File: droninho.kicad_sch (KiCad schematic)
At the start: 36 parts, among them J2 M2, J3 M1, J4 M3, J5 M4, J6 I2C, J7 TXD0/RXD0, J8 I2C, Q1 SI2300, Q2 SI2300, Q3 SI2300, Q4 SI2300, U1 AMS1117-3.3, U2 MPU9250/6500, U3 ESP32 Dev Kit

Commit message: update
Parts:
- removed H1, H2: MountingHole_Pad_Power, MountingHole:MountingHole_2.2mm_M2_Pad_TopBottom, symbol Mechanical:MountingHole_Pad_Power
- added H3, H4: MountingHole_Pad_Power, MountingHole:MountingHole_2.2mm_M2_Pad_TopBottom, symbol Library:MountingHole_Pad_Power
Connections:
- net BAT+: now also H3.1
- net GND: now also H4.1
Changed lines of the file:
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@@
-	)
-	(symbol
-		(lib_id "Mechanical:MountingHole_Pad_Power")
-		(at 34.29 91.44 90)
-		(unit 1)
-		(exclude_from_sim yes)
-		(in_bom no)
-		(on_board yes)
-		(dnp no)
-		(fields_autoplaced yes)
-		(property "Reference" "H1"
-			(at 33.02 85.09 90)
-			(effects
-				(font
-					(size 1.27 1.27)
-				)
-			)
-		)
-		(property "Value" "MountingHole_Pad_Power"
-			(at 33.02 87.63 90)
-			(effects
-				(font
-					(size 1.27 1.27)
-				)
-			)
-		)
-		(property "Footprint" "MountingHole:MountingHole_2.2mm_M2_Pad_TopBottom"
-			(at 34.29 91.44 0)
-			(effects
-				(font
-					(size 1.27 1.27)
-				)
-				(hide yes)
-			)
-		)
-		(property "Datasheet" "~"
-			(at 34.29 91.44 0)
-			(effects
-				(font
-					(size 1.27 1.27)
-				)
-				(hide yes)
-			)
-		)
-		(property "Description" "Mounting Hole with connection"
-			(at 34.29 91.44 0)
-			(effects
-				(font
-					(size 1.27 1.27)
-				)
-				(hide yes)
-			)
-		)
-		(pin "1"
-		)
-		(instances
-			(project ""
-				(path "/50215636-8ce2-4b01-ade7-3715bffabe9d"
-					(reference "H1")
-					(unit 1)
-				)
-			)
-		)
 	)
 	(symbol
@@
 	)
 	(symbol
+		(lib_id "Library:MountingHole_Pad_Power")
+		(at 34.29 104.14 90)
+		(unit 1)
+		(exclude_from_sim no)
+		(in_bom no)
+		(on_board yes)
+		(dnp no)
+		(fields_autoplaced yes)
+		(property "Reference" "H4"
+			(at 33.02 97.79 90)
+			(effects
+				(font
+					(size 1.27 1.27)
+				)
+			)
+		)
+		(property "Value" "MountingHole_Pad_Power"
+			(at 33.02 100.33 90)
+			(effects
+				(font
+					(size 1.27 1.27)
+				)
+			)
+		)
+		(property "Footprint" "MountingHole:MountingHole_2.2mm_M2_Pad_TopBottom"
+			(at 34.29 104.14 0)
+			(effects
+				(font
+					(size 1.27 1.27)
+				)
+				(hide yes)
+			)
+		)
+		(property "Datasheet" "~"
+			(at 34.29 104.14 0)
+			(effects
+				(font
+					(size 1.27 1.27)
+				)
+				(hide yes)
+			)
+		)
+		(property "Description" "Mounting Hole with connection"
+			(at 34.29 104.14 0)
+			(effects
+				(font
+					(size 1.27 1.27)
+				)
+				(hide yes)
+			)
+		)
+		(pin "1"
+		)
+		(instances
+			(project "droninho"
+				(path "/50215636-8ce2-4b01-ade7-3715bffabe9d"
+					(reference "H4")
+					(unit 1)
+				)
+			)
+		)
+	)
+	(symbol
 		(lib_id "power:GND")
 		(at 29.21 55.88 0)
@@
 	)
 	(symbol
-		(lib_id "Mechanical:MountingHole_Pad_Power")
-		(at 34.29 104.14 90)
-		(unit 1)
-		(exclude_from_sim yes)
-		(in_bom no)
-		(on_board yes)
-		(dnp no)
-		(fields_autoplaced yes)
-		(property "Reference" "H2"
-			(at 33.02 97.79 90)
-			(effects
-				(font
-					(size 1.27 1.27)
-				)
-			)
-		)
-		(property "Value" "MountingHole_Pad_Power"
-			(at 33.02 100.33 90)
-			(effects
-				(font
-					(size 1.27 1.27)
-				)
-			)
-		)
-		(property "Footprint" "MountingHole:MountingHole_2.2mm_M2_Pad_TopBottom"
-			(at 34.29 104.14 0)
-			(effects
-				(font
-					(size 1.27 1.27)
-				)
-				(hide yes)
-			)
-		)
-		(property "Datasheet" "~"
-			(at 34.29 104.14 0)
-			(effects
-				(font
-					(size 1.27 1.27)
-				)
-				(hide yes)
-			)
-		)
-		(property "Description" "Mounting Hole with connection"
-			(at 34.29 104.14 0)
-			(effects
-				(font
-					(size 1.27 1.27)
-				)
-				(hide yes)
-			)
-		)
-		(pin "1"
-		)
-		(instances
-			(project "droninho"
-				(path "/50215636-8ce2-4b01-ade7-3715bffabe9d"
-					(reference "H2")
-					(unit 1)
-				)
-			)
-		)
-	)
-	(symbol
 		(lib_id "power:GND")
 		(at 213.36 144.78 90)
@@
 					(unit 1)
 				)
+			)
+		)
+	)
+	(symbol
+		(lib_id "Library:MountingHole_Pad_Power")
+		(at 34.29 91.44 90)
+		(unit 1)
+		(exclude_from_sim no)
+		(in_bom no)
+		(on_board yes)
+		(dnp no)
+		(fields_autoplaced yes)
+		(property "Reference" "H3"
+			(at 33.02 85.09 90)
+			(effects
+				(font
+					(size 1.27 1.27)
+				)
+			)
+		)
+		(property "Value" "MountingHole_Pad_Power"
+			(at 33.02 87.63 90)
+			(effects
+				(font
+					(size 1.27 1.27)
+				)
+			)
+		)
+		(property "Footprint" "MountingHole:MountingHole_2.2mm_M2_Pad_TopBottom"
+			(at 34.29 91.44 0)
+			(effects
+				(font
+					(size 1.27 1.27)
+				)
+				(hide yes)
+			)
+		)
+		(property "Datasheet" "~"
+			(at 34.29 91.44 0)
+			(effects
+				(font
+					(size 1.27 1.27)
+				)
+				(hide yes)
+			)
+		)
+		(property "Description" "Mounting Hole with connection"
+			(at 34.29 91.44 0)
+			(effects
+				(font
+					(size 1.27 1.27)
+				)
+				(hide yes)
+			)
+		)
+		(pin "1"
+		)
+		(instances
+			(project ""
+				(path "/50215636-8ce2-4b01-ade7-3715bffabe9d"
+					(reference "H3")
+					(unit 1)
+				)

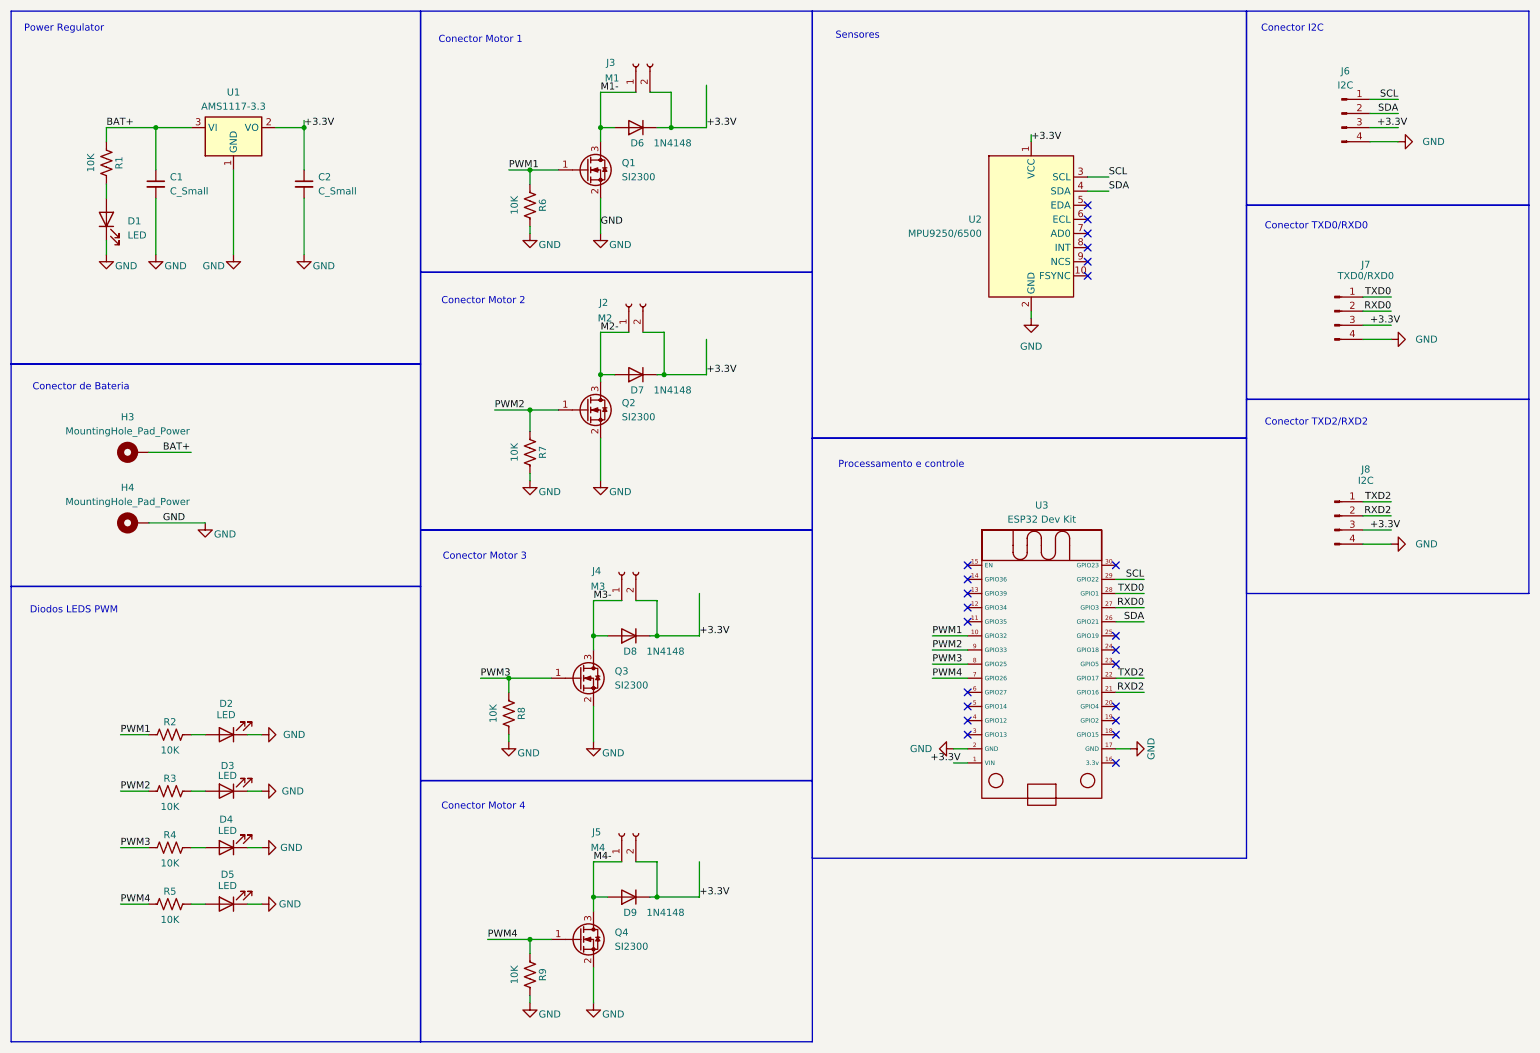
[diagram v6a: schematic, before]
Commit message: pull-down resistors removed, change leds positions.
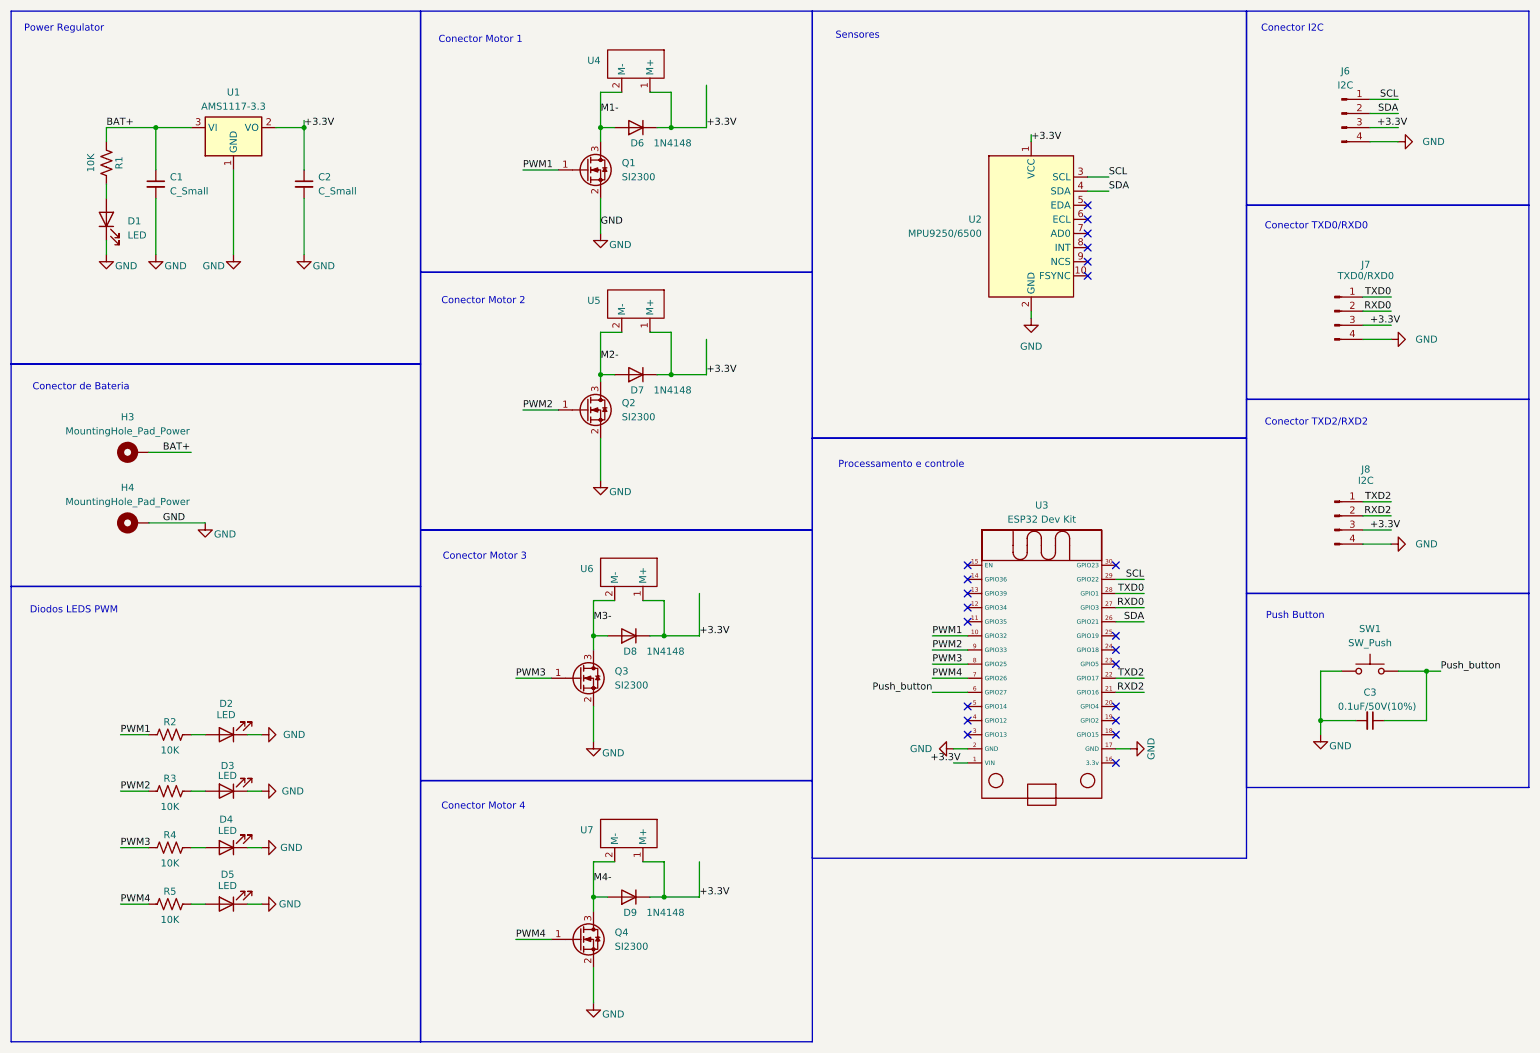
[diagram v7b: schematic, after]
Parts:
- removed J2: M2, Connector_JST:JST_PH_B2B-PH-K_1x02_P2.00mm_Vertical, symbol Connector:Conn_01x02_Socket
- removed J3: M1, Connector_JST:JST_PH_B2B-PH-K_1x02_P2.00mm_Vertical, symbol Connector:Conn_01x02_Socket
- removed J4: M3, Connector_JST:JST_PH_B2B-PH-K_1x02_P2.00mm_Vertical, symbol Connector:Conn_01x02_Socket
- removed J5: M4, Connector_JST:JST_PH_B2B-PH-K_1x02_P2.00mm_Vertical, symbol Connector:Conn_01x02_Socket
- removed R6, R7, R8, R9: 10K, Resistor_SMD:R_0805_2012Metric_Pad1.20x1.40mm_HandSolder, symbol Device:R_US
- added C3: 0.1uF/50V(10%), Capacitor_SMD:C_0805_2012Metric_Pad1.18x1.45mm_HandSolder, symbol Device:C_Small
- added SW1: SW_Push, Button_Switch_SMD:SW_Push_1P1T_NO_CK_KMR2, symbol Switch:SW_Push
- added U4, U5, U6, U7: ~, Library:Connector_Motor, symbol Library:Connector_Motor
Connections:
- net +3.3V: now also U4.1 (M+), U5.1 (M+), U6.1 (M+), U7.1 (M+)
- net GND: now also C3.2, SW1.1
- net M1-: now also U4.2 (M-)
- net M2-: now also U5.2 (M-)
- net M3-: now also U6.2 (M-)
- net M4-: now also U7.2 (M-)
- net Push_button: now reaches U3.6 (GPIO27)
- net Push_button: now also C3.1, SW1.2
- no-connect marks 23 -> 22
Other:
- note added: "Push Button"

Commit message: packages updated
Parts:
- C1, C2: value C_Small -> 22uF/10V(20%); Package (none) -> C_0805_2012Metric_Pad1.18x1.45mm_HandSolder
- C3: Package (none) -> C_0805_2012Metric_Pad1.18x1.45mm_HandSolder
- D1: value LED -> RED LED; Package (none) -> LED_0805_2012Metric_Pad1.15x1.40mm_HandSolder
- D2, D3, D4, D5: value LED -> WHITE LED; Package (none) -> LED_0805_2012Metric_Pad1.15x1.40mm_HandSolder
- D6, D7, D8, D9: value 1N4148 -> 1N4148W SOD-123 SMD 100V 2A (A2); Package (none) -> D_SOD-123
- J6, J7, J8: Package (none) -> PinHeader_1x04_P2.54mm_Vertical
- Q1, Q2, Q3, Q4: value SI2300 -> Si2300DS; Package (none) -> SOT-23
- R1, R2, R3, R4, R5: value 10K -> 10K(5%); Package (none) -> R_0805_2012Metric_Pad1.20x1.40mm_HandSolder
- SW1: value SW_Push -> KMR241G LFS; Package (none) -> SW_Push_1P1T_NO_CK_KMR2
- U1: Package (none) -> SOT-223-3_TabPin2
- U2: Package (none) -> Not applicable
- U3: value ESP32 Dev Kit -> ESP32 ESP-WROOM-32 DEVKit V1; Package (none) -> Not applicable
- U4, U5, U6, U7: value ~ -> Through Hole Connector; Package (none) -> Not applicable
